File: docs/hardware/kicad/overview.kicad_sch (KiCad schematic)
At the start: 0 parts

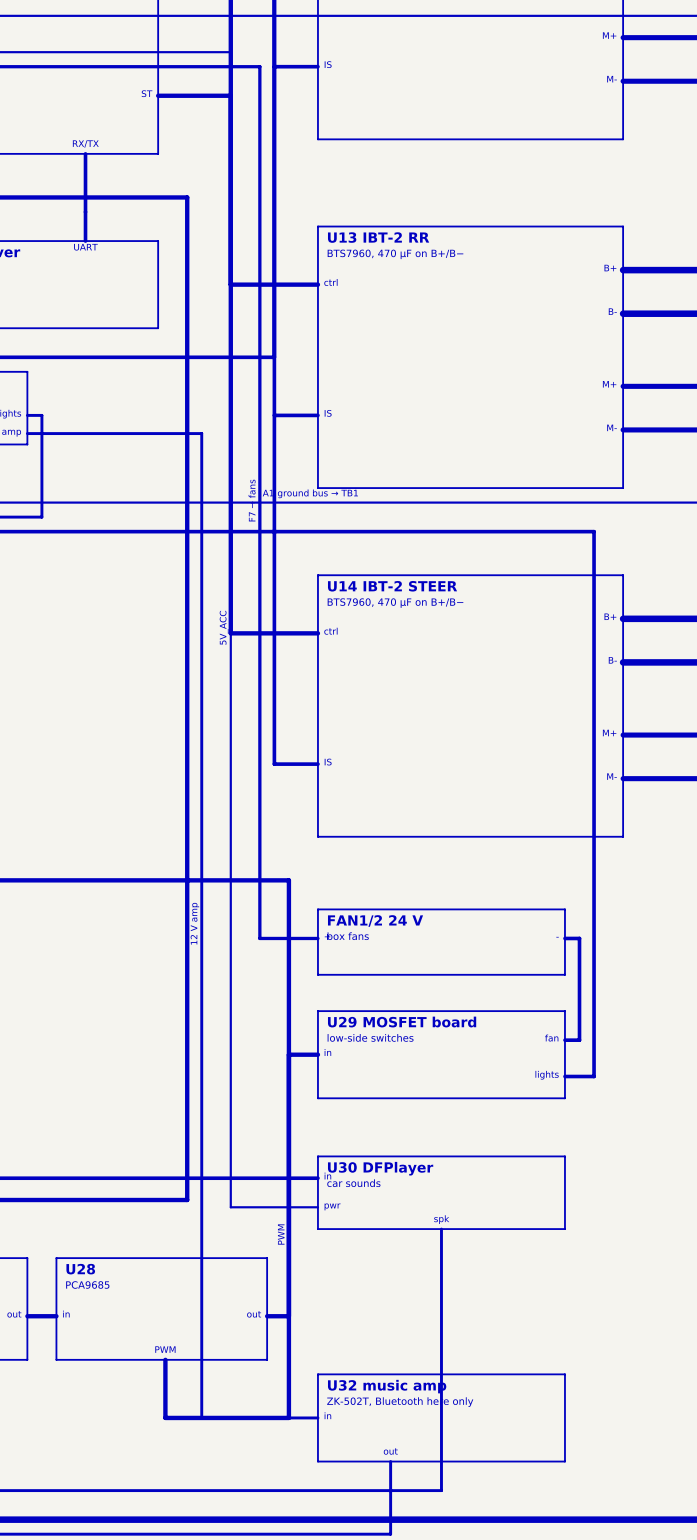
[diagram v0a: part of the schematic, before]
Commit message: Add the listen-only Bluetooth log module
An HC-06 module (U33) hears TX0, the USB serial log, through a 1k
resistor (R29); its TXD is not connected, so nothing on a phone can reach
the ESP32, whose own Wi-Fi and Bluetooth stay off. An Android phone reads
the live log with a serial terminal app.

The phone can't type, so holding the horn for 3 s with the car Locked or
Killed and stopped prints a full report: status, fault table, crash copy
and the last 50 records. `report` on the console does the same. The
trigger is in rideon_core with tests, under SR-31, plus a mutant.

New bt_setup bench firmware sets the module to 115200 baud and a PIN
before it goes in the box. Schematic, wire list, BOM, overview and the 3D
view are regenerated; BLUETOOTH.md, PINOUT, WIRING, SAFETY, README and a
phase 3 commissioning gate describe it.

Co-Authored-By: Claude Opus 5.5 <noreply@anthropic.com>
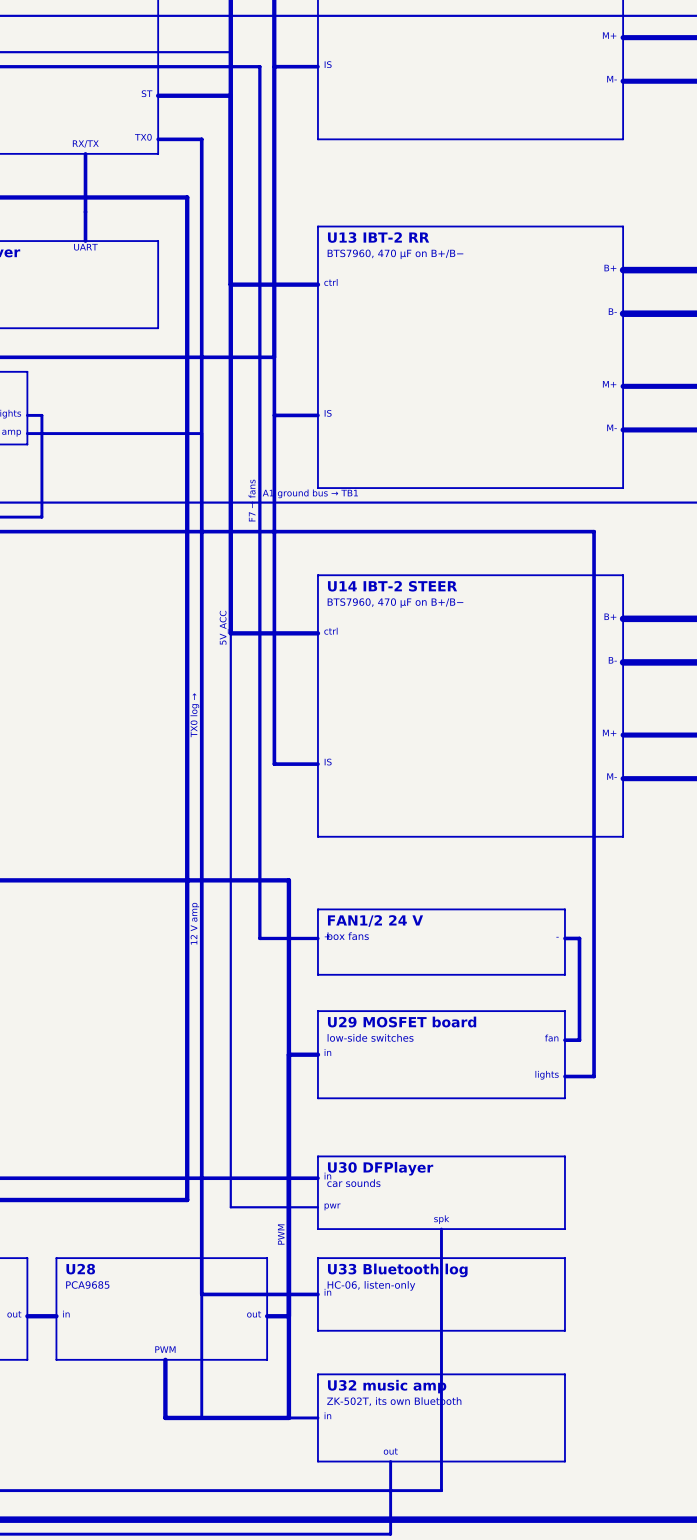
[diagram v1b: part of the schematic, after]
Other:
- note added: "HC-06, listen-only"
- note added: "TX0"
- note added: "TX0 log →"
- note added: "U33 Bluetooth log"
- note added: "ZK-502T, its own Bluetooth"
- note removed: "ZK-502T, Bluetooth here only"
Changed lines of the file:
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@@
 (text "RR" (exclude_from_sim no) (at 307.2 155 0) (effects (font (size 0.9 0.9)) (justify right)))
 (text "ST" (exclude_from_sim no) (at 307.2 170 0) (effects (font (size 0.9 0.9)) (justify right)))
+(text "TX0" (exclude_from_sim no) (at 307.2 176 0) (effects (font (size 0.9 0.9)) (justify right)))
 (rectangle (start 268 190) (end 308 202) (stroke (width 0.25) (type solid) (color 120 0 0 1)) (fill (type color) (color 255 255 225 1)))
 (text "U21 ELRS receiver" (exclude_from_sim no) (at 269.2 191 0) (effects (font (size 1.4 1.4) (bold yes)) (justify left top)))
@@
 (text "lights" (exclude_from_sim no) (at 289.2 214 0) (effects (font (size 0.9 0.9)) (justify right)))
 (text "amp" (exclude_from_sim no) (at 289.2 216.5 0) (effects (font (size 0.9 0.9)) (justify right)))
+(rectangle (start 330 330) (end 364 340) (stroke (width 0.25) (type solid) (color 120 0 0 1)) (fill (type color) (color 255 255 225 1)))
+(text "U33 Bluetooth log" (exclude_from_sim no) (at 331.2 331 0) (effects (font (size 1.4 1.4) (bold yes)) (justify left top)))
+(text "HC-06, listen-only" (exclude_from_sim no) (at 331.2 333.4 0) (effects (font (size 1.0 1.0)) (justify left top)))
+(text "in" (exclude_from_sim no) (at 330.8 335 0) (effects (font (size 0.9 0.9)) (justify left)))
 (rectangle (start 330 346) (end 364 358) (stroke (width 0.25) (type solid) (color 120 0 0 1)) (fill (type color) (color 255 255 225 1)))
 (text "U32 music amp" (exclude_from_sim no) (at 331.2 347 0) (effects (font (size 1.4 1.4) (bold yes)) (justify left top)))
-(text "ZK-502T, Bluetooth here only" (exclude_from_sim no) (at 331.2 349.4 0) (effects (font (size 1.0 1.0)) (justify left top)))
+(text "ZK-502T, its own Bluetooth" (exclude_from_sim no) (at 331.2 349.4 0) (effects (font (size 1.0 1.0)) (justify left top)))
 (text "in" (exclude_from_sim no) (at 330.8 352 0) (effects (font (size 0.9 0.9)) (justify left)))
 (text "out" (exclude_from_sim no) (at 340 357.4 0) (effects (font (size 0.9 0.9)) (justify bottom)))
@@
 (polyline (pts (xy 258 182) (xy 266 182) (xy 266 319) (xy 330 319)) (stroke (width 0.5) (type solid) (color 110 110 110 1)) (fill (type none)))
 (text "SOUND_TX" (exclude_from_sim no) (at 265.5 250.5 90) (effects (font (size 0.9 0.9) (color 110 110 110 1)) (justify bottom)))
+(polyline (pts (xy 308 176) (xy 314 176) (xy 314 335) (xy 330 335)) (stroke (width 0.5) (type solid) (color 110 110 110 1)) (fill (type none)))
+(text "TX0 log →" (exclude_from_sim no) (at 313.5 255.5 90) (effects (font (size 0.9 0.9) (color 110 110 110 1)) (justify bottom)))
 (polyline (pts (xy 347 326) (xy 347 362) (xy 172 362) (xy 172 300) (xy 154 300)) (stroke (width 0.4) (type solid) (color 60 60 60 1)) (fill (type none)))
 (text "alert speaker" (exclude_from_sim no) (at 259.5 361.5 0) (effects (font (size 0.9 0.9) (color 60 60 60 1)) (justify bottom)))

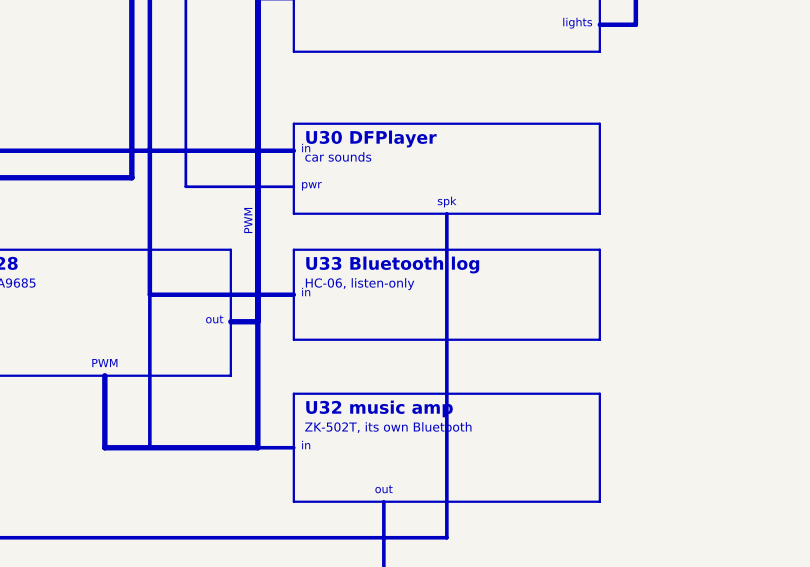
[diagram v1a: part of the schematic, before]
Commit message: Switch the Bluetooth log module to BLE (HM-10) for iPhone and Android
The HC-06 is Bluetooth Classic, which iPhones can't use. The HM-10 (CC2541)
is BLE, which both iPhone and Android support. Same wiring: RXD on TX0
through R29, TXD not connected.

bt_setup now speaks the HM-10 dialect (genuine and the common clones):
finds the baud rate, names it RideOn, sets 115200, restarts it and checks.
No PIN: HM-10 pairing PINs are unreliable on iPhones and clones, and the
log holds no personal data.

A BLE link passes on about 2 KB/s, so the horn-triggered report prints one
line per 100 ms. A typed report on USB stays at full speed.

Co-Authored-By: Claude Opus 5.5 <noreply@anthropic.com>
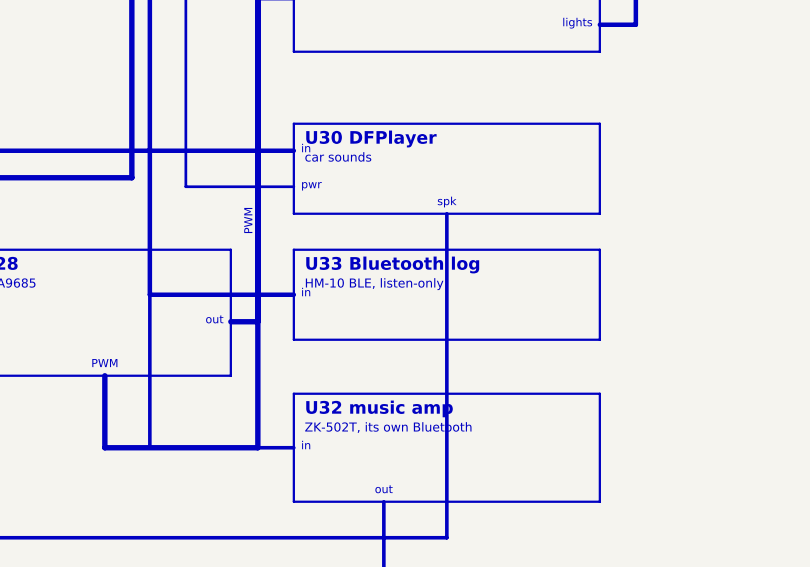
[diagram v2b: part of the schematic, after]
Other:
- note added: "HM-10 BLE, listen-only"
- note removed: "HC-06, listen-only"
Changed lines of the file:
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@@
 (rectangle (start 330 330) (end 364 340) (stroke (width 0.25) (type solid) (color 120 0 0 1)) (fill (type color) (color 255 255 225 1)))
 (text "U33 Bluetooth log" (exclude_from_sim no) (at 331.2 331 0) (effects (font (size 1.4 1.4) (bold yes)) (justify left top)))
-(text "HC-06, listen-only" (exclude_from_sim no) (at 331.2 333.4 0) (effects (font (size 1.0 1.0)) (justify left top)))
+(text "HM-10 BLE, listen-only" (exclude_from_sim no) (at 331.2 333.4 0) (effects (font (size 1.0 1.0)) (justify left top)))
 (text "in" (exclude_from_sim no) (at 330.8 335 0) (effects (font (size 0.9 0.9)) (justify left)))
 (rectangle (start 330 346) (end 364 358) (stroke (width 0.25) (type solid) (color 120 0 0 1)) (fill (type color) (color 255 255 225 1)))
